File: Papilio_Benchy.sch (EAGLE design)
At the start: 121 parts, among them IC1 FT2232H, SW1 SWITCH-2CH-6P-3010010P1, SW2 EVQQ2, T100 MOSFET-NCHANNELSMD, U1 ARDUINO_MEGA_SHIELD, U100 PCA9306, U101 ATMEGA32U4-XUMU, U2 LTC3419EMS, U3 93C46B, X1 12MHz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

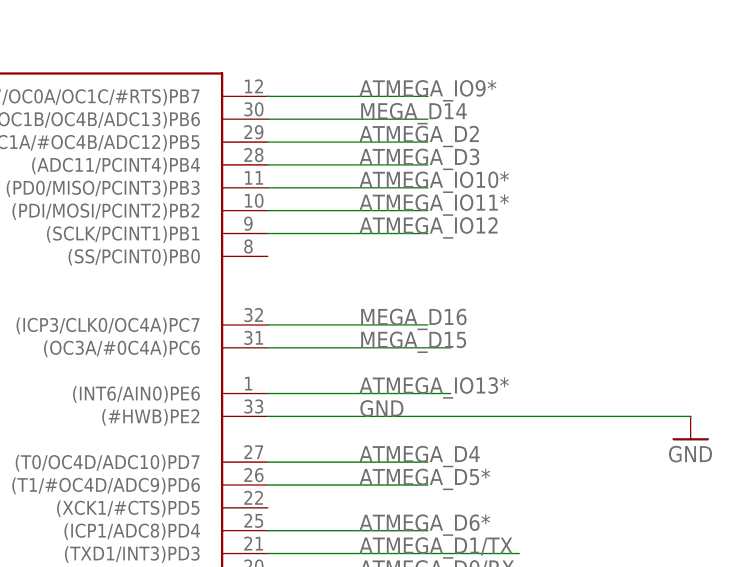
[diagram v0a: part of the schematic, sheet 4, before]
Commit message: SPI pins moved to same location as the Uno
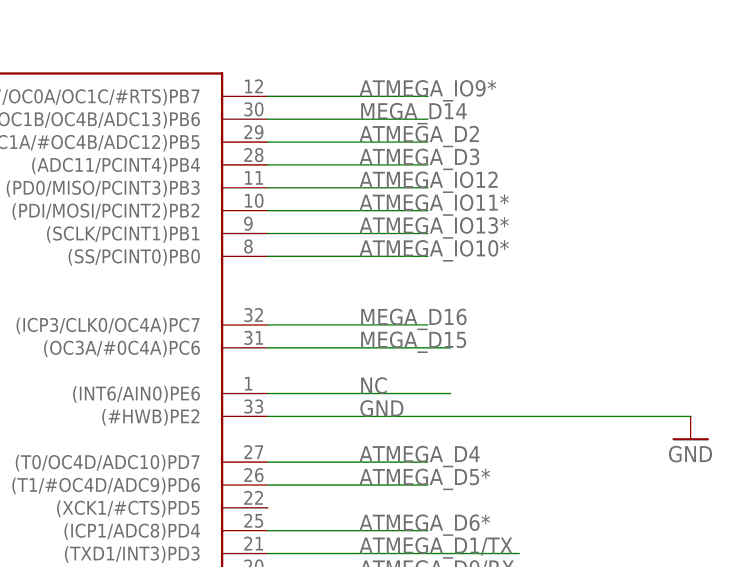
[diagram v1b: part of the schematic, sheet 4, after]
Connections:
- new net NC: U101.(INT6/AIN0)PE6
- net ATMEGA_IO10*: now also U101.(SS/PCINT0)PB0; no longer U101.(PD0/MISO/PCINT3)PB3
- net ATMEGA_IO12: now also U101.(PD0/MISO/PCINT3)PB3; no longer U101.(SCLK/PCINT1)PB1
- net ATMEGA_IO13*: now also U101.(SCLK/PCINT1)PB1; no longer U101.(INT6/AIN0)PE6
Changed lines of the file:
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@@
 <net name="ATMEGA_IO12" class="0">
 <segment>
-<pinref part="U101" gate="G$1" pin="(SCLK/PCINT1)PB1"/>
-<wire x1="53.34" y1="111.76" x2="71.12" y2="111.76" width="0.1524" layer="91"/>
-<label x="63.5" y="111.76" size="1.778" layer="95"/>
+<pinref part="U101" gate="G$1" pin="(PD0/MISO/PCINT3)PB3"/>
+<wire x1="53.34" y1="116.84" x2="71.12" y2="116.84" width="0.1524" layer="91"/>
+<label x="63.5" y="116.84" size="1.778" layer="95"/>
 </segment>
 </net>
@@
 </segment>
 <segment>
-<wire x1="73.66" y1="93.98" x2="53.34" y2="93.98" width="0.1524" layer="91"/>
-<label x="63.5" y="93.98" size="1.778" layer="95"/>
-<pinref part="U101" gate="G$1" pin="(INT6/AIN0)PE6"/>
+<pinref part="U101" gate="G$1" pin="(SCLK/PCINT1)PB1"/>
+<wire x1="53.34" y1="111.76" x2="71.12" y2="111.76" width="0.1524" layer="91"/>
+<label x="63.5" y="111.76" size="1.778" layer="95"/>
 </segment>
 </net>
@@
 <net name="ATMEGA_IO10*" class="0">
 <segment>
-<pinref part="U101" gate="G$1" pin="(PD0/MISO/PCINT3)PB3"/>
-<wire x1="53.34" y1="116.84" x2="71.12" y2="116.84" width="0.1524" layer="91"/>
-<label x="63.5" y="116.84" size="1.778" layer="95"/>
+<pinref part="U101" gate="G$1" pin="(SS/PCINT0)PB0"/>
+<wire x1="53.34" y1="109.22" x2="71.12" y2="109.22" width="0.1524" layer="91"/>
+<label x="63.5" y="109.22" size="1.778" layer="95"/>
 </segment>
 </net>
@@
 </segment>
 </net>
+<net name="NC" class="0">
+<segment>
+<wire x1="73.66" y1="93.98" x2="53.34" y2="93.98" width="0.1524" layer="91"/>
+<label x="63.5" y="93.98" size="1.778" layer="95"/>
+<pinref part="U101" gate="G$1" pin="(INT6/AIN0)PE6"/>
+</segment>
+</net>

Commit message: Change HSWAP so I/O floats during config. Cleanup schematic sheets.
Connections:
- net 3V3: now also S1B0.IO_L1P_HSWAPEN_0
- net GND: no longer S1B0.IO_L1P_HSWAPEN_0
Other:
- note added: "Arduino Section"
- note added: "Copyright 2014 Gadget Factory, LLC"
- note added: "FT2232H Section"
- note added: "HSWAP to 3.3V to float all pins during configuration"
- note added: "M0 is connected to 3.3V"
- note added: "M1 is connected to GND"
- note added: "PROG_B asserting PROG_B causes a JTAG reconfiguration"
- note added: "Power Connections"
- note added: "This section is derived from the Arduino Leonardo Design and has the same license."
- note added: "This section is from the Pipistrello design with permission from Magnus."
- note added: "This work is licensed under the Creative Commons Attribution Share-Alike License."
- note added: "This work is licensed under the Creative Commons Attribution-ShareAlike License."
- note added: "VCCAUX requires 3.3V"
- note removed: "HSWAP (H1_10) to ground to pull up all pins during configuration"
- note removed: "M0 (H2_2) is connected to VCCO_2"
- note removed: "M1(H1_39) is connected to GND"
- note removed: "M2 (H1_38) is connected to VCCO_2"
- note removed: "PROG_B (C12) asserting PROG_B caused a JTAG reconfiguration"
- note removed: "QUESTION: Reset switch control FPGA and Arduino? Or just FPGA and Arduino reset under FPGA control..."
- note removed: "RPAR is a reverse current shunt for 3.3V JTAG."
- note removed: "TODO: If this switch is too big or not practical during routing then make it smaller surface mount part or remove it."
- note removed: "This work is licensed under the Creative Commons Attribution-NonCommercial-ShareAlike License."
- note removed: "This work is licensed under the Creative Commons Non-Commercial Attribution License."
- note removed: "VCCAUX requires 2.5V"
- moved on the sheet: FLASH, SW1

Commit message: Final fixes as pointed out in the forum.
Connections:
- net 3V3: now also U1.IOREF; no longer U1.3V3@3, U1.3V3@4
- net 5V0: now also U1.5V@1, U1.5V@2
- net GND: no longer U1.GND@5, U1.GND@6
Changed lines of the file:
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@@
 <part name="FRAME6" library="frames" deviceset="LETTER_L" device=""/>
 <part name="FRAME7" library="frames" deviceset="TABL_L" device=""/>
+<part name="5V0_PWR1" library="Bogdan_Commons" deviceset="5V0" device=""/>
 </parts>
 <sheets>
@@
 <instance part="GND7" gate="1" x="-281.94" y="-2.54"/>
 <instance part="3V3_PWR12" gate="A" x="-281.94" y="7.62"/>
-<instance part="3V3_PWR13" gate="A" x="-53.34" y="111.76"/>
+<instance part="3V3_PWR13" gate="A" x="-60.96" y="111.76"/>
 <instance part="GND12" gate="1" x="-325.12" y="0" rot="MR0"/>
 <instance part="3V3_PWR17" gate="A" x="-325.12" y="10.16" rot="MR0"/>
 <instance part="3V3_PWR18" gate="A" x="35.56" y="81.28" rot="R90"/>
+<instance part="5V0_PWR1" gate="A" x="-50.8" y="119.38"/>
 </instances>
 <busses>
@@
 </segment>
 <segment>
-<pinref part="U1" gate="ARDUINO_MEGA" pin="GND@6"/>
-<pinref part="U1" gate="ARDUINO_MEGA" pin="GND@5"/>
-<wire x1="-45.72" y1="63.5" x2="-45.72" y2="66.04" width="0.1524" layer="91"/>
 <wire x1="-45.72" y1="81.28" x2="-45.72" y2="78.74" width="0.2032" layer="91"/>
 <wire x1="-45.72" y1="78.74" x2="-45.72" y2="76.2" width="0.2032" layer="91"/>
@@
 <pinref part="U1" gate="ARDUINO_MEGA" pin="GND@4"/>
 <pinref part="U1" gate="ARDUINO_MEGA" pin="GND@3"/>
-<wire x1="-45.72" y1="66.04" x2="-45.72" y2="68.58" width="0.1524" layer="91"/>
-<junction x="-45.72" y="66.04"/>
-<junction x="-45.72" y="63.5"/>
 </segment>
 <segment>
@@
 <pinref part="3V3_PWR13" gate="A" pin="3V3"/>
 <pinref part="U1" gate="ARDUINO_MEGA" pin="3V3@1"/>
-<wire x1="-53.34" y1="109.22" x2="-45.72" y2="109.22" width="0.1524" layer="91"/>
+<wire x1="-60.96" y1="109.22" x2="-45.72" y2="109.22" width="0.1524" layer="91"/>
 <pinref part="U1" gate="ARDUINO_MEGA" pin="3V3@2"/>
 <wire x1="-45.72" y1="109.22" x2="-45.72" y2="106.68" width="0.1524" layer="91"/>
-<pinref part="U1" gate="ARDUINO_MEGA" pin="3V3@3"/>
-<wire x1="-45.72" y1="106.68" x2="-45.72" y2="104.14" width="0.1524" layer="91"/>
-<pinref part="U1" gate="ARDUINO_MEGA" pin="3V3@4"/>
-<wire x1="-45.72" y1="104.14" x2="-45.72" y2="101.6" width="0.1524" layer="91"/>
 <junction x="-45.72" y="109.22"/>
+<pinref part="U1" gate="ARDUINO_MEGA" pin="IOREF"/>
+<wire x1="-45.72" y1="106.68" x2="-45.72" y2="96.52" width="0.1524" layer="91"/>
 <junction x="-45.72" y="106.68"/>
-<junction x="-45.72" y="104.14"/>
-<junction x="-45.72" y="101.6"/>
 </segment>
 <segment>
@@
 <wire x1="-50.8" y1="88.9" x2="-45.72" y2="88.9" width="0.1524" layer="91"/>
 </segment>
-</net>
+<segment>
+<pinref part="U1" gate="ARDUINO_MEGA" pin="5V@1"/>
+<pinref part="5V0_PWR1" gate="A" pin="5V0"/>
+<wire x1="-50.8" y1="116.84" x2="-45.72" y2="116.84" width="0.1524" layer="91"/>
+<pinref part="U1" gate="ARDUINO_MEGA" pin="5V@2"/>
+<wire x1="-45.72" y1="114.3" x2="-45.72" y2="116.84" width="0.1524" layer="91"/>
+<junction x="-45.72" y="116.84"/>
+</segment>
+</net>
